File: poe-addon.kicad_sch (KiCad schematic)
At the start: 14 parts, among them U1 25AA02E48T-I_OT, X1 0813-1X1T-57-F, X2 Conn_01x05_Male, X3 Conn_01x05_Male

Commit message: add pg02s 3D model
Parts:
- X2, X3: footprint Connector_PinSocket_2.54mm:PinSocket_1x05_P2.54mm_Vertical -> Connector_PinHeader_2.54mm:PinHeader_1x05_P2.54mm_Vertical
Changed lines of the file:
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@@
       (effects (font (size 1.27 1.27)) hide)
     )
-    (property "Footprint" "Connector_PinSocket_2.54mm:PinSocket_1x05_P2.54mm_Vertical" (id 2) (at 161.29 78.74 0)
+    (property "Footprint" "Connector_PinHeader_2.54mm:PinHeader_1x05_P2.54mm_Vertical" (id 2) (at 161.29 78.74 0)
       (effects (font (size 1.27 1.27)) hide)
     )
@@
       (effects (font (size 1.27 1.27)) hide)
     )
-    (property "Footprint" "Connector_PinSocket_2.54mm:PinSocket_1x05_P2.54mm_Vertical" (id 2) (at 195.58 78.74 0)
+    (property "Footprint" "Connector_PinHeader_2.54mm:PinHeader_1x05_P2.54mm_Vertical" (id 2) (at 195.58 78.74 0)
       (effects (font (size 1.27 1.27)) hide)
     )
@@
     )
     (path "/00000000-0000-0000-0000-00005bf9f5ee/00000000-0000-0000-0000-000059e7c1ef"
-      (reference "U3") (unit 1) (value "PG02S4803A") (footprint "AlexComponents:PG02S")
+      (reference "U3") (unit 1) (value "PG02S4803A") (footprint "newam:PG02S")
     )
     (path "/00000000-0000-0000-0000-00005bfa08a0/00000000-0000-0000-0000-00005c1faae5"
@@
     )
     (path "/a301cd7a-869e-41c4-af8d-0d9e595bd70e"
-      (reference "X2") (unit 1) (value "Conn_01x05_Male") (footprint "Connector_PinSocket_2.54mm:PinSocket_1x05_P2.54mm_Vertical")
+      (reference "X2") (unit 1) (value "Conn_01x05_Male") (footprint "Connector_PinHeader_2.54mm:PinHeader_1x05_P2.54mm_Vertical")
     )
     (path "/650d4e5d-41b8-44d6-9b3a-2b4481fa83e2"
-      (reference "X3") (unit 1) (value "Conn_01x05_Male") (footprint "Connector_PinSocket_2.54mm:PinSocket_1x05_P2.54mm_Vertical")
+      (reference "X3") (unit 1) (value "Conn_01x05_Male") (footprint "Connector_PinHeader_2.54mm:PinHeader_1x05_P2.54mm_Vertical")
     )
     (path "/00000000-0000-0000-0000-00005bfa08a0/00000000-0000-0000-0000-00005b95f795"

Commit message: 10nF 0603: 1276-1921-1-ND -> 1276-1009-1-ND
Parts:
- C2, C4: DigiKey Part Number 1276-1921-1-ND -> 1276-1009-1-ND
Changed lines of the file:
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@@
       (effects (font (size 1.27 1.27)) hide)
     )
-    (property "DigiKey Part Number" "1276-1921-1-ND" (id 4) (at 68.58 116.84 90)
+    (property "DigiKey Part Number" "1276-1009-1-ND" (id 4) (at 68.58 116.84 90)
       (effects (font (size 1.27 1.27)) hide)
     )
@@
       (effects (font (size 1.27 1.27)) hide)
     )
-    (property "DigiKey Part Number" "1276-1921-1-ND" (id 4) (at 76.2 113.03 90)
+    (property "DigiKey Part Number" "1276-1009-1-ND" (id 4) (at 76.2 113.03 90)
       (effects (font (size 1.27 1.27)) hide)
     )

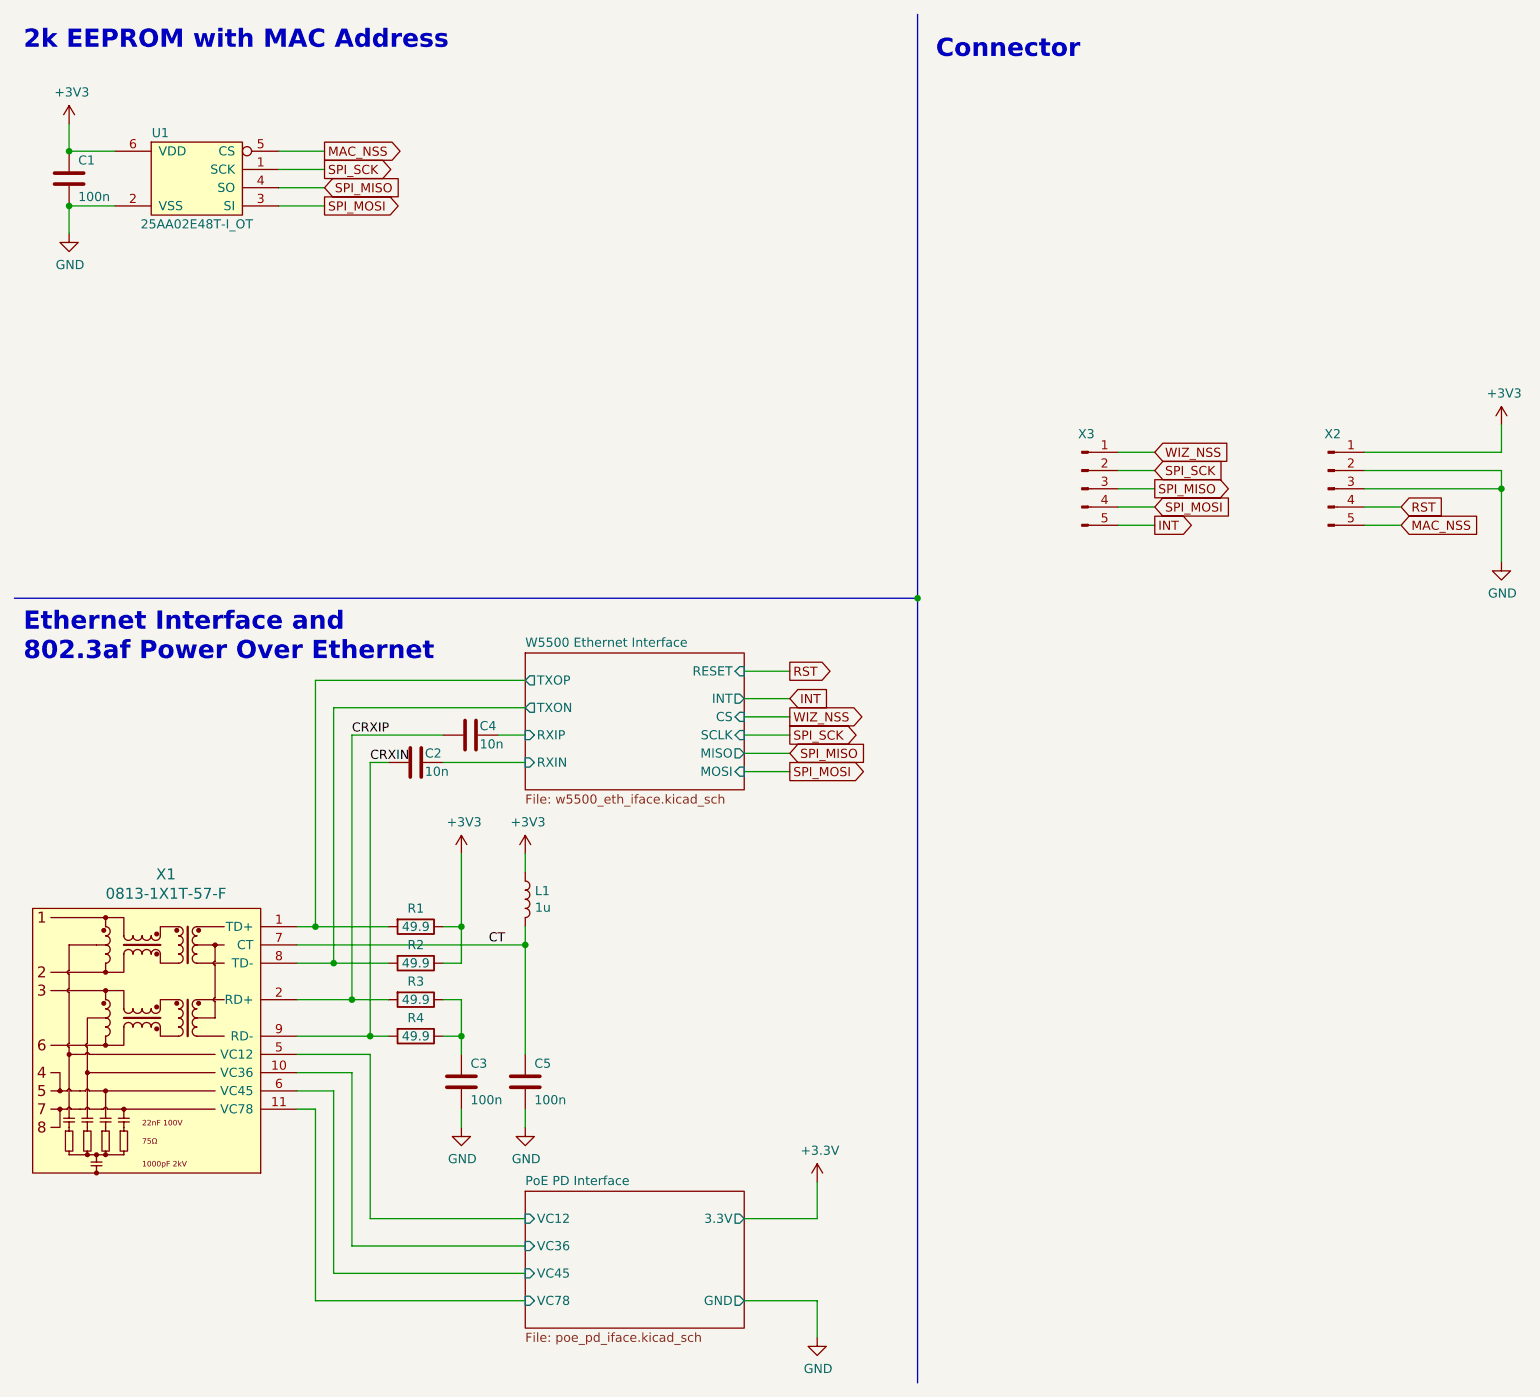
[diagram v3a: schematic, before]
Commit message: add mounting holes, replace magjack with in-stock part
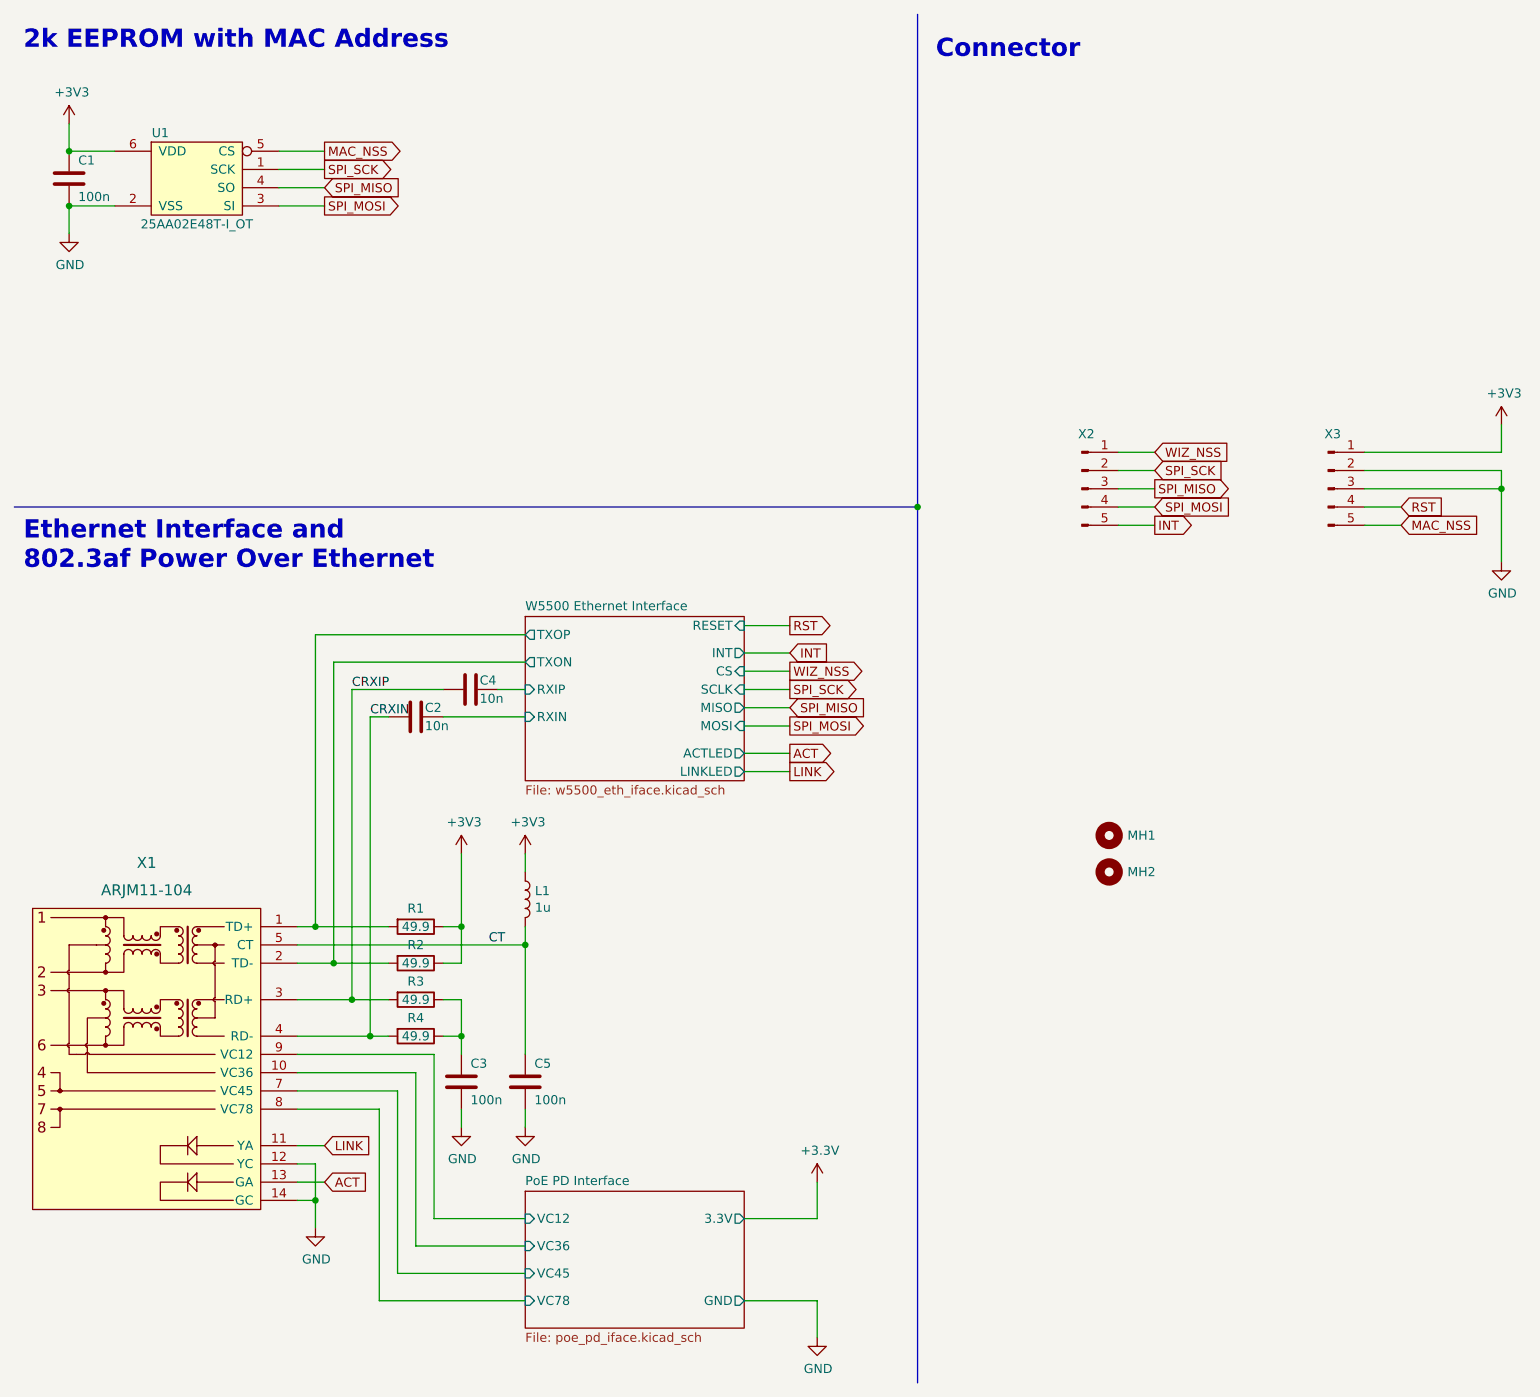
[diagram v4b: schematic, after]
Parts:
- removed X1: 0813-1X1T-57-F, newam:0813-1X1T-57-F_RJ45-Jack, symbol newam:0813-1X1T-57-F
- added MH1, MH2: MountingHole, MountingHole:MountingHole_3.2mm_M3, symbol Mechanical:MountingHole
- added X1: ARJM11-104, newam:ARJM11D7-104-AB-EW2, symbol newam:ARJM11-104
- renumbered X3 to X2, X2 to X3
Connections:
- net CRXIN: now also X1.4 (RD-)
- net CRXIP: now also X1.3 (RD+)
- net CT: now also X1.5 (CT)
- net GND: now also X1.12 (YC), X1.14 (GC)
- net PoE PD Interface/VC12: now also X1.9 (VC12)
- net PoE PD Interface/VC36: now also X1.10 (VC36)
- net PoE PD Interface/VC45: now also X1.7 (VC45)
- net PoE PD Interface/VC78: now also X1.8 (VC78)
- net W5500 Ethernet Interface/TXON: now also X1.2 (TD-)
- net W5500 Ethernet Interface/TXOP: now also X1.1 (TD+)
- new net ACT: X1.13 (GA)
- new net LINK: X1.11 (YA)
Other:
- sheet W5500 Ethernet Interface ports: added ACTLED, LINKLED; removed none
- moved on the sheet: C2, C4
